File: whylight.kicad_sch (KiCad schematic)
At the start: 84 parts, among them J1 USB device, J2 External 12v, J3 LoRa, J4 I2C, J5 UART, J6 LED strip, U1 AG5412, U2 KPC357NT0ATLD, U3 ESP32-C6-WROOM-1, U4 Ra-01, U5 W5500, U6 AP63203WU, U7 USBLC6-2P6, U8 74LVC1G125, U9 L78L05_SOT89, Y1 25MHz

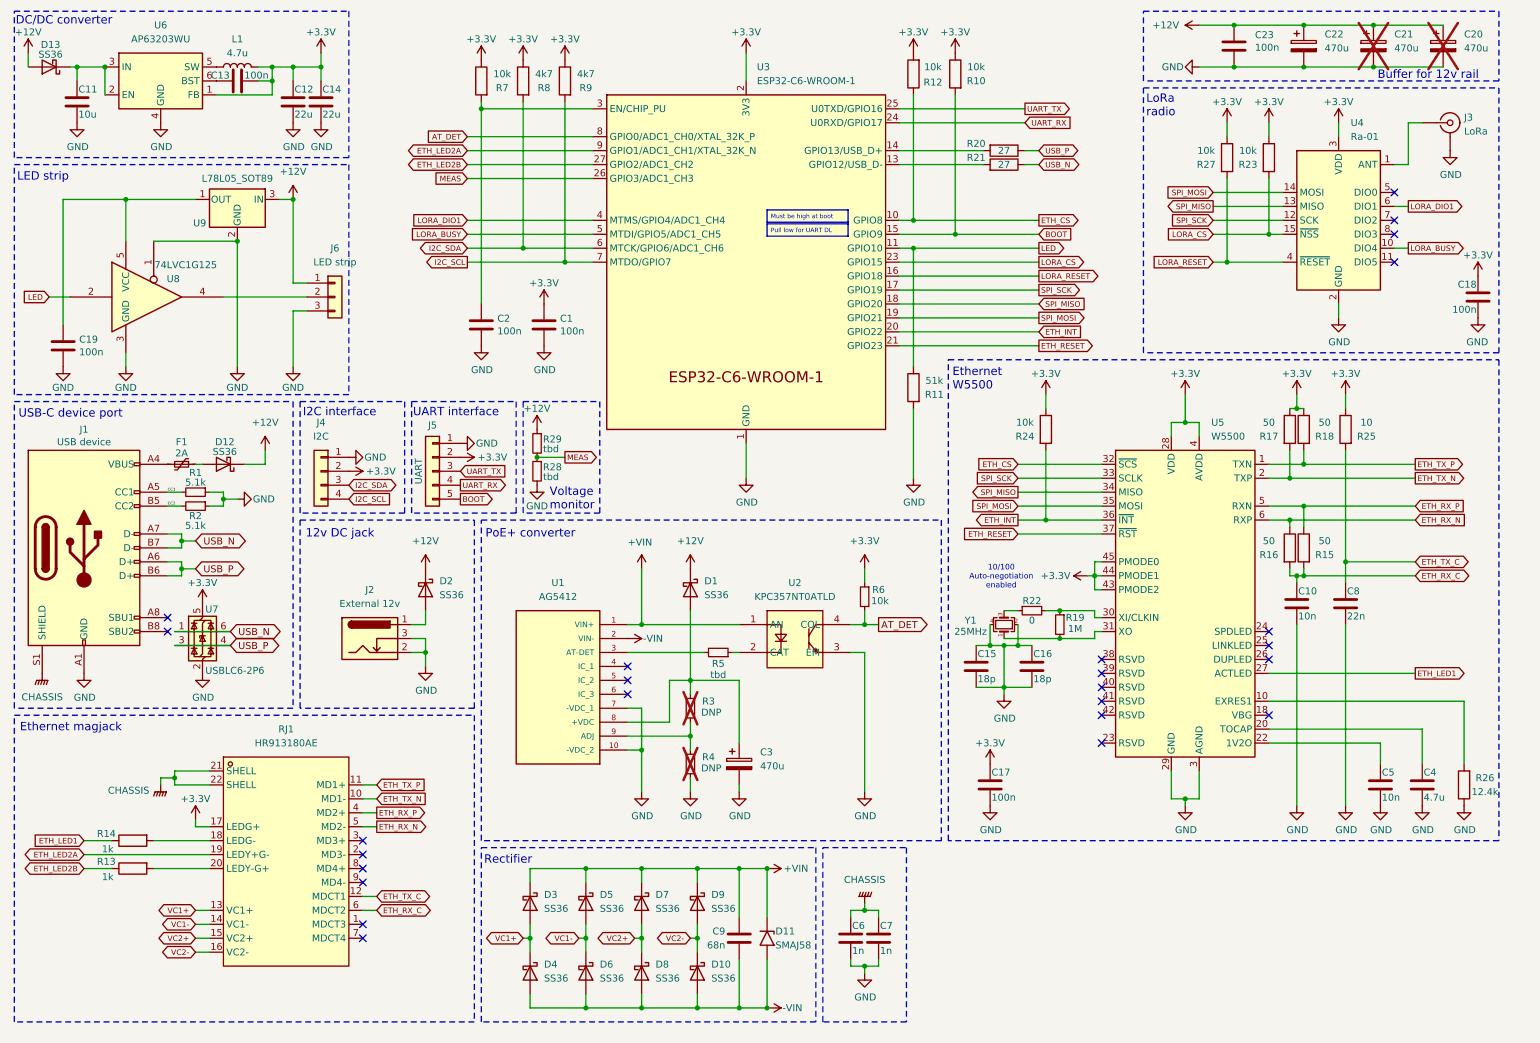
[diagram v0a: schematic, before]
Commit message: Fixes & add voltage/current monitor chip
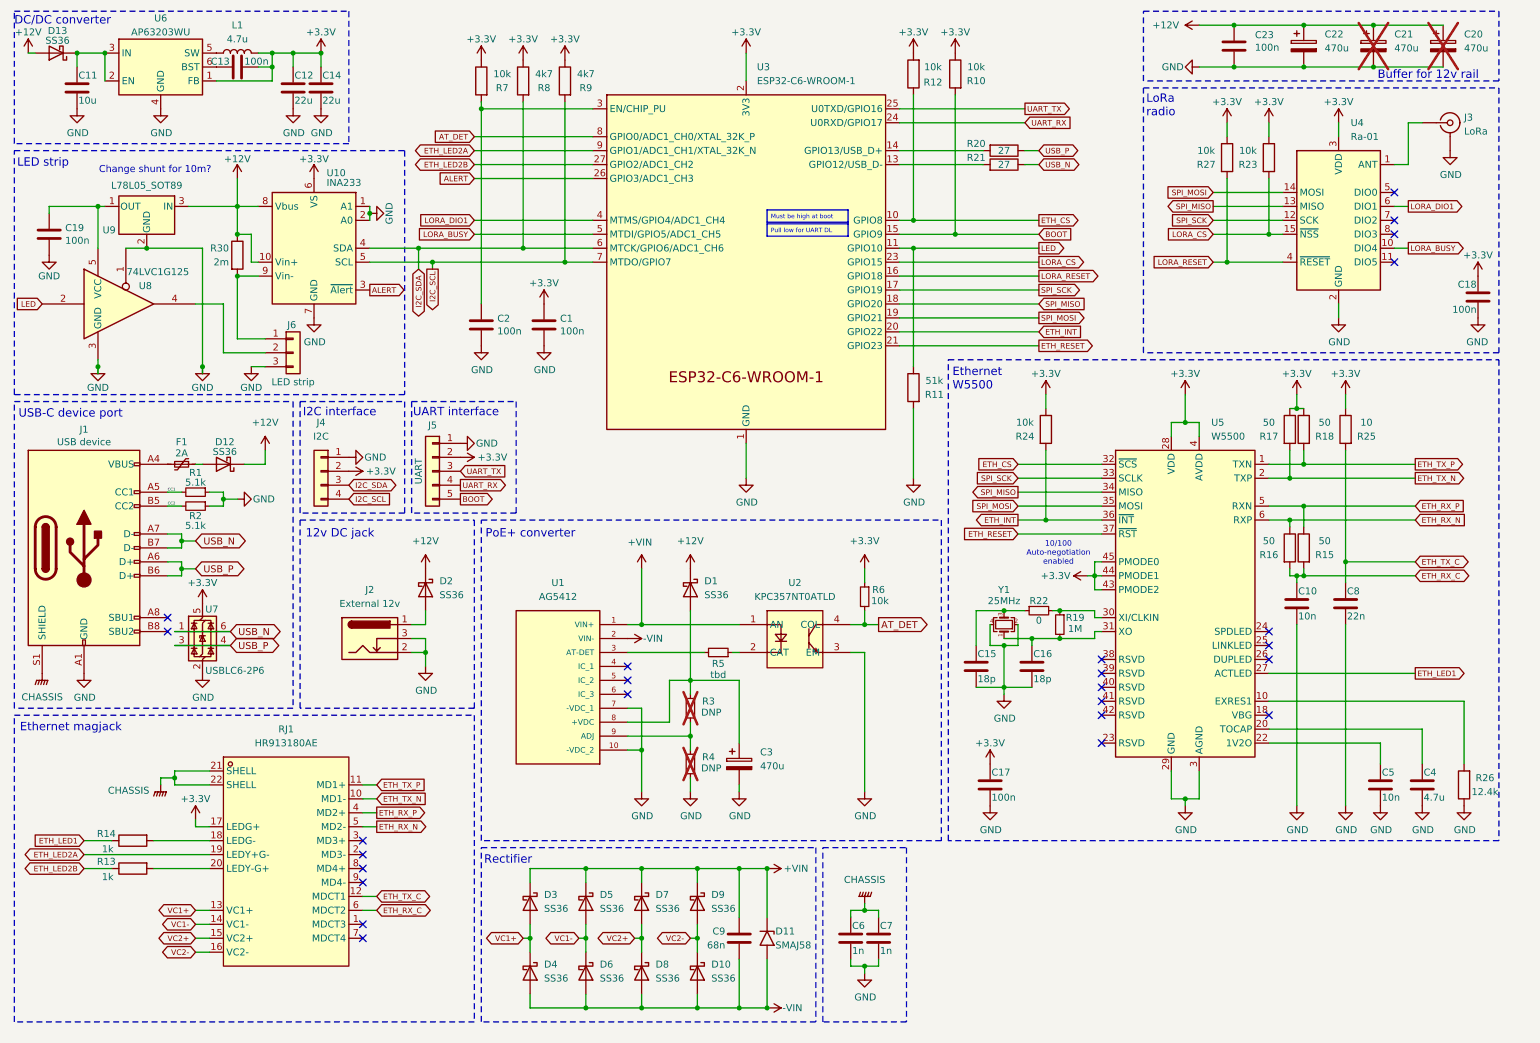
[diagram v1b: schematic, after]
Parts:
- removed R28, R29: tbd, Resistor_SMD:R_0402_1005Metric, symbol Device:R_Small
- added R30: 2m, symbol Device:R
- added U10: INA233, Package_SO:VSSOP-10_3x3mm_P0.5mm, symbol Sensor_Energy:INA233
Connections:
- net +12V: now also R30.1, U10.10 (Vin+), U10.8 (Vbus); no longer J6.1 (Pin_1)
- net +3.3V: now also U10.6 (VS)
- net GND: now also U10.1 (A1), U10.2 (A0), U10.7 (GND); no longer C15.1, C16.1
- net I2C_SCL: now also U10.5 (SCL)
- net I2C_SDA: now also U10.4 (SDA)
- net at R19.2, U5.31 (XO), Y1.1: now also C16.1
- net at R22.1, Y1.3: now also C15.1
- net MEAS renamed ALERT
- net ALERT: now also U10.3 (~{Alert})
- new net: J6.1 (Pin_1), R30.2, U10.9 (Vin-)
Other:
- note added: "Change shunt for 10m?"
- note removed: "Voltage monitor"
- moved on the sheet: C11, C12, C13, C14, C19, D13, J6, L1, R22, U6, U8, U9

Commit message: Stuff.
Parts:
- removed C10, C5: 10n, Capacitor_SMD:C_0402_1005Metric, symbol Device:C
- removed C15, C16: 18p, Capacitor_SMD:C_1206_3216Metric, symbol Device:C
- removed C17: 100n, Capacitor_SMD:C_0402_1005Metric, symbol Device:C
- removed C21, C3: 470u, symbol Device:C_Polarized
- removed C4: 4.7u, Capacitor_SMD:C_0402_1005Metric, symbol Device:C
- removed C6: 1n, Capacitor_SMD:C_1206_3216Metric, symbol Device:C
- removed C8: 22n, Capacitor_SMD:C_0402_1005Metric, symbol Device:C
- removed C9: 68n, symbol Device:C
- removed D10, D12, D13, D9: SS36, Diode_SMD:D_SMA, symbol Diode:SS36
- removed D11: SMAJ58, Diode_SMD:D_SMA, symbol Diode:SMAJ58A
- removed J2: External 12v, Connector_BarrelJack:BarrelJack_GCT_DCJ200-10-A_Horizontal, symbol Connector:Barrel_Jack_Switch
- removed J3: LoRa, SparkFun-Connector:SMA-EDGE, symbol SparkFun-RF:SMA_EdgeMount
- removed J6: LED strip, symbol Connector_Generic:Conn_01x03
- removed R13, R14: 1k, Resistor_SMD:R_0402_1005Metric, symbol symbols:R
- removed R15, R16, R17, R18: 50, Resistor_SMD:R_0402_1005Metric, symbol symbols:R
- removed R19: 1M, Resistor_SMD:R_0402_1005Metric, symbol Device:R_Small
- removed R22: 0, Resistor_SMD:R_0402_1005Metric, symbol Device:R_Small
- removed R24: 10k, Resistor_SMD:R_0402_1005Metric, symbol symbols:R
- removed R25: 10, Resistor_SMD:R_0402_1005Metric, symbol symbols:R
- removed R26: 12.4k, Resistor_SMD:R_0402_1005Metric, symbol symbols:R
- removed RJ1: HR913180AE, library:RJ45-TH_HR913180AE, symbol RJ45-TH_HR913180AE:HR913180AE
- removed U5: W5500, Package_QFP:LQFP-48_7x7mm_P0.5mm, symbol Interface_Ethernet:W5500
- removed U9: L78L05_SOT89, Package_TO_SOT_SMD:SOT-89-3, symbol Regulator_Linear:L78L05_SOT89
- removed Y1: 25MHz, Crystal:Crystal_SMD_3225-4Pin_3.2x2.5mm, symbol Device:Crystal_GND24_Small
- added C21, C24: 100n, Capacitor_SMD:C_0402_1005Metric, symbol symbols:C
- added C3: 68n, Capacitor_SMD:C_0402_1005Metric, symbol Device:C
- added C9: 470u, Capacitor_SMD:CP_Elec_8x10, symbol Device:C_Polarized
- added D10, D11: TVS, symbol SparkFun-DiscreteSemi:D_TVS
- added D9: SMAJ58, Diode_SMD:D_SMA, symbol Diode:SMAJ58A
- added F2: 10A, Fuse:Fuse_0805_2012Metric, symbol mch2021-rescue:Polyfuse_Small-Device
- added J2: External 5v, TerminalBlock_Altech:Altech_AK100_1x02_P5.00mm, symbol Connector:Screw_Terminal_01x02
- added J3: External 5v, Connector_BarrelJack:BarrelJack_GCT_DCJ200-10-A_Horizontal, symbol Connector:Barrel_Jack_Switch
- added J6: LoRa, Connector_Coaxial:SMA_Amphenol_901-143_Horizontal, symbol Connector:Conn_Coaxial
- added J7: Ledstrip, TerminalBlock_Altech:Altech_AK100_1x04_P5.00mm, symbol Connector:Screw_Terminal_01x04
- added JP1: Power source, symbol Jumper:Jumper_3_Open
- added JP2: LED logic, symbol Jumper:Jumper_3_Open
- added R28: 51k, Resistor_SMD:R_0402_1005Metric, symbol symbols:R
- added R29: 100, Resistor_SMD:R_0402_1005Metric, symbol symbols:R
- added U11: L78L05_SOT89, Package_TO_SOT_SMD:SOT-89-3, symbol Regulator_Linear:L78L05_SOT89
- added U9: 74LVC1G125, Package_TO_SOT_SMD:SOT-353_SC-70-5, symbol buffer:74LVC1G125
- C1, C19: LCSC C307331 -> C394158
- C11: value 10u -> 22u
- C13, C18, C23: LCSC (none) -> C394158
- C2: value 100n -> 1u; LCSC C307331 -> C5137485
- C20: footprint (none) -> Capacitor_SMD:CP_Elec_8x10; LCSC (none) -> C2164331; now fitted; now in the parts list
- C22: footprint (none) -> Capacitor_SMD:CP_Elec_8x10; LCSC (none) -> C2164331
- C7: LCSC (none) -> C2173292
- J4: footprint (none) -> Connector_JST:JST_SH_SM04B-SRSS-TB_1x04-1MP_P1.00mm_Horizontal; symbol Connector_Generic:Conn_01x04 -> Connector_Generic_MountingPin:Conn_01x04_MountingPin
- J5: footprint (none) -> Connector_PinHeader_2.54mm:PinHeader_1x06_P2.54mm_Vertical; symbol Connector_Generic:Conn_01x05 -> Connector_Generic:Conn_01x06
- R23: value 10k -> 1k
- R27: value 10k -> 100
- R30: value 2m -> 10m; footprint (none) -> Resistor_SMD:R_1206_3216Metric
- R5: value tbd -> 1k
- R6, R7: LCSC (none) -> C60490
- U1: value AG5412 -> AG5405; Availability In Stock -> (none); Check_prices https://www.snapeda.com/parts/Ag5300/Silvertel/view-part/?r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 -> (none); DESCRIPTION Power-over-Ethernet Plus Module -> (none); Description_1 Isolated PoE Module DC DC Converter Output 12V 2.5A 36V - 5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 -> (none); HEIGHT 14mm -> (none); MANUFACTURER_NAME Silvertel -> (none); MANUFACTURER_PART_NUMBER AG5300 -> (none); MF Silvertel -> (none); MOUSER_PART_NUMBER 480-AG5300 -> (none); MOUSER_PRICE-STOCK https://www.mouser.co.uk/ProductDetail/Silvertel/Ag5300?qs=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 -> (none); MP Ag5300 -> (none); Package None -> (none); Price None -> (none); Purchase-URL https://www.snapeda.com/api/url_track_click_mouser/?unipart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 -> (none); SnapEDA_Link https://www.snapeda.com/parts/Ag5300/Silvertel/view-part/?r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 -> (none)
- U2: LCSC (none) -> C136410; LCSC Part C136410 -> (none)
- U8: symbol 74xGxx:74LVC1G125 -> buffer:74LVC1G125
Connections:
- net -VIN is gone; now on an unnamed net: D4.2 (A), D6.2 (A), D8.2 (A), U1.2 (VIN-)
- net +3.3V: no longer R23.1, R27.1
- net +VIN: now also R30.1, U10.10 (Vin+), U10.8 (Vbus), D10.1 (A1), F2.1, JP1.3 (B), U11.3 (IN); no longer D3.1 (K), D5.1 (K), D7.1 (K), U1.1 (VIN+), U2.1 (AN)
- net AT_DET: now also U3.11 (GPIO10); no longer U3.8 (GPIO0/ADC1_CH0/XTAL_32K_P)
- net ETH_INT: now also U3.4 (MTMS/GPIO4/ADC1_CH4); no longer U3.20 (GPIO22)
- net ETH_LED2A: now also R11.1, U3.17 (GPIO19); no longer U3.9 (GPIO1/ADC1_CH1/XTAL_32K_N)
- net GND: now also C19.1, J4.MP (MountPin), C21.2, C24.1, C9.2, D10.2 (A2), D11.2 (A2), J2.1 (Pin_1), J3.2, J3.3, J6.2 (Ext), J7.4 (Pin_4), R28.2, U11.2 (GND), U9.1, U9.3 (GND); no longer C19.2
- net LORA_BUSY: now also U3.19 (GPIO21); no longer U3.5 (MTDI/GPIO5/ADC1_CH5)
- net LORA_CS: no longer R23.2
- net LORA_DIO1: now also U3.20 (GPIO22); no longer U3.4 (MTMS/GPIO4/ADC1_CH4)
- net LORA_RESET: now also R28.1; no longer R27.2
- net SPI_MISO: now also U3.8 (GPIO0/ADC1_CH0/XTAL_32K_P); no longer U3.18 (GPIO20)
- net SPI_MOSI: now also U3.5 (MTDI/GPIO5/ADC1_CH5); no longer U3.19 (GPIO21)
- net SPI_SCK: now also U3.9 (GPIO1/ADC1_CH1/XTAL_32K_N); no longer U3.17 (GPIO19)
- net UART_RX: now also R23.1; no longer U3.24 (U0RXD/GPIO17)
- net VC1+: now also D1.2 (A), D2.1 (K); no longer D3.2 (A), D4.1 (K)
- net VC1-: now also D3.2 (A), D4.1 (K); no longer D5.2 (A), D6.1 (K)
- net VC2+: now also D5.2 (A), D6.1 (K); no longer D7.2 (A), D8.1 (K)
- net VC2-: now also D7.2 (A), D8.1 (K)
- net VLED: now reaches R30.2, U10.9 (Vin-)
- net VLED: now also C20.1, C22.1, C23.1, J7.1 (Pin_1)
- net at U8.4: now also R29.1
- net at C11.1, U6.2 (EN), U6.3 (IN): now also JP1.2 (C)
- net at R3.2, U1.8 (+VDC): now also C9.1, F2.2, J2.2 (Pin_2), J3.1; no longer D1.2 (A)
- net +5V: now reaches U8.5 (VCC)
- net +5V: now also C19.2, C24.2, JP2.2 (C), U9.5 (VCC); no longer C19.1
- net at D2.2 (A): now also C3.2, D9.2 (A2)
- net at U4.1 (ANT): now also J6.1 (In)
- net +5v-USB: now reaches F1.1
- net +5v-USB: now also D11.1 (A1), JP1.1 (A), JP2.3 (B)
- net EN: now reaches C2.1, R7.2, U3.3 (EN/CHIP_PU)
- net EN: now also J5.6 (Pin_6)
- removed net +12V: C20.1, C22.1, C23.1, D1.1 (K), D2.1 (K), R30.1, U10.10 (Vin+), U10.8 (Vbus)
- net CHASSIS: no longer names the net of C7.1, J1.S1 (SHIELD)
- removed net LED: R11.1, U3.11 (GPIO10), U8.2
- new net: C21.1, JP2.1 (A), U11.1 (OUT)
- new net: J7.3 (Pin_3), R27.1
- new net: R27.2, U9.4
- new net: J7.2 (Pin_2), R29.2
- new net: C3.1, D1.1 (K), D3.1 (K), D5.1 (K), D7.1 (K), D9.1 (A1), U1.1 (VIN+), U2.1 (AN)
- new net LCLK: R23.2, U3.24 (U0RXD/GPIO17), U9.2
- new net LDAT: U3.18 (GPIO20), U8.2
- no-connect marks 25 -> 9
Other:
- added sheet Ethernet (ethernet.kicad_sch)
- note added: "Choose between USB and ext / PoE power"
- note added: "DC/DC converter for logic"
- note added: "Do NOT backfeed power into the PoE module. Install only one of the connectors or the PoE module but not multiple!"
- note added: "Ethernet"
- note added: "I2C & UART"
- note added: "LDO for LED data logic voltage"
- note added: "Microcontroller"
- note added: "PoE+ & external power"
- note added: "Power measurement"
- note removed: "10/100 Auto-negotiation enabled"
- note removed: "12v DC jack"
- note removed: "Buffer for 12v rail"
- note removed: "Change shunt for 10m?"
- note removed: "DC/DC converter"
- note removed: "Ethernet W5500"
- note removed: "Ethernet magjack"
- note removed: "I2C interface"
- note removed: "LED strip"
- note removed: "PoE+ converter"
- note removed: "Rectifier"
- note removed: "UART interface"
- moved on the sheet: C1, C12, C13, C14, C18, C19, C2, C22, C23, F1, J1, L1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

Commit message: Stuff.
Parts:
- removed F2: 10A, Fuse:Fuse_0805_2012Metric, symbol mch2021-rescue:Polyfuse_Small-Device
- removed J6: LoRa, Connector_Coaxial:SMA_Amphenol_901-143_Horizontal, symbol Connector:Conn_Coaxial
- C11, C12, C14: footprint Capacitor_SMD:C_0402_1005Metric -> Capacitor_SMD:C_0805_2012Metric; LCSC (none) -> C45783
- D1, D2, D3, D4, D5, D6, D7, D8: LCSC (none) -> C727061
- D10, D11: value TVS -> 5.5v; footprint (none) -> Diode_SMD:D_SOD-323; LCSC (none) -> C19224
- D9: LCSC (none) -> C132935
- J2: footprint TerminalBlock_Altech:Altech_AK100_1x02_P5.00mm -> Connector_Phoenix_MC_HighVoltage:PhoenixContact_MC_1,5_2-G-5.08_1x02_P5.08mm_Horizontal; LCSC (none) -> -; now not fitted; now left out of the parts list
- J3, J5, U1: LCSC (none) -> -; now not fitted; now left out of the parts list
- J4: LCSC (none) -> C160404
- J7: footprint TerminalBlock_Altech:Altech_AK100_1x04_P5.00mm -> Connector_Phoenix_MC_HighVoltage:PhoenixContact_MC_1,5_4-GF-5.08_1x04_P5.08mm_Horizontal_ThreadedFlange_MountHole; LCSC (none) -> -; now not fitted; now left out of the parts list
- JP1, JP2: footprint (none) -> Jumper:SolderJumper-3_P1.3mm_Open_RoundedPad1.0x1.5mm_NumberLabels; LCSC (none) -> -
- U10: LCSC (none) -> C2653838
- U11: LCSC (none) -> C408272
- U4: value Ra-01 -> Ra-01SH; LCSC (none) -> -; now not fitted; now left out of the parts list
- U6: LCSC (none) -> C780769
- U7: LCSC (none) -> C2827693
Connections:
- net +VIN: now also C9.1, J2.2 (Pin_2), J3.1, R3.2, U1.8 (+VDC)
- no-connect marks 9 -> 10
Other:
- note added: "U.FL connector on-board"

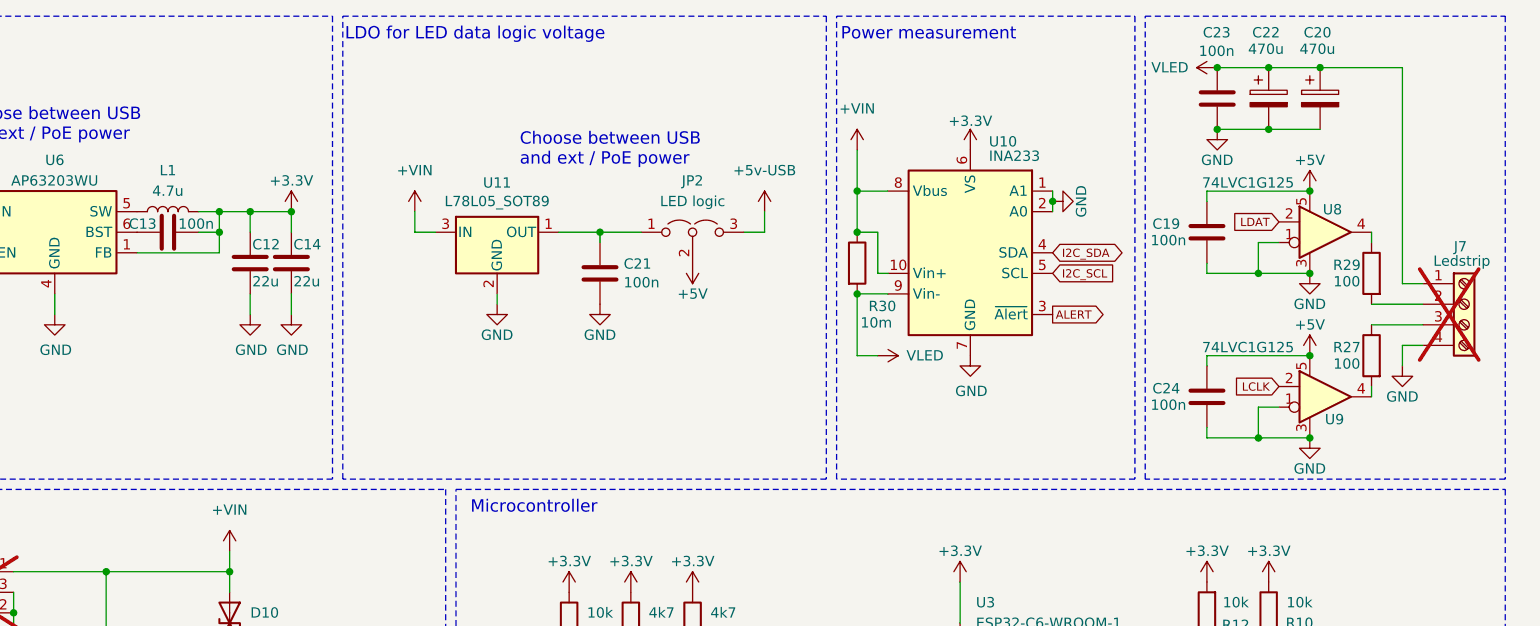
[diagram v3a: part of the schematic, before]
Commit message: added 3D models, added LCSC numbers, added caps in RX line ethernet as per the datasheet, change crystal and capacitors to correctly match w5500 as per the datasheet, added bead to filter analoge power supply for w5500 as per the datasheet, added filter for the ina2XX for beter monitoring
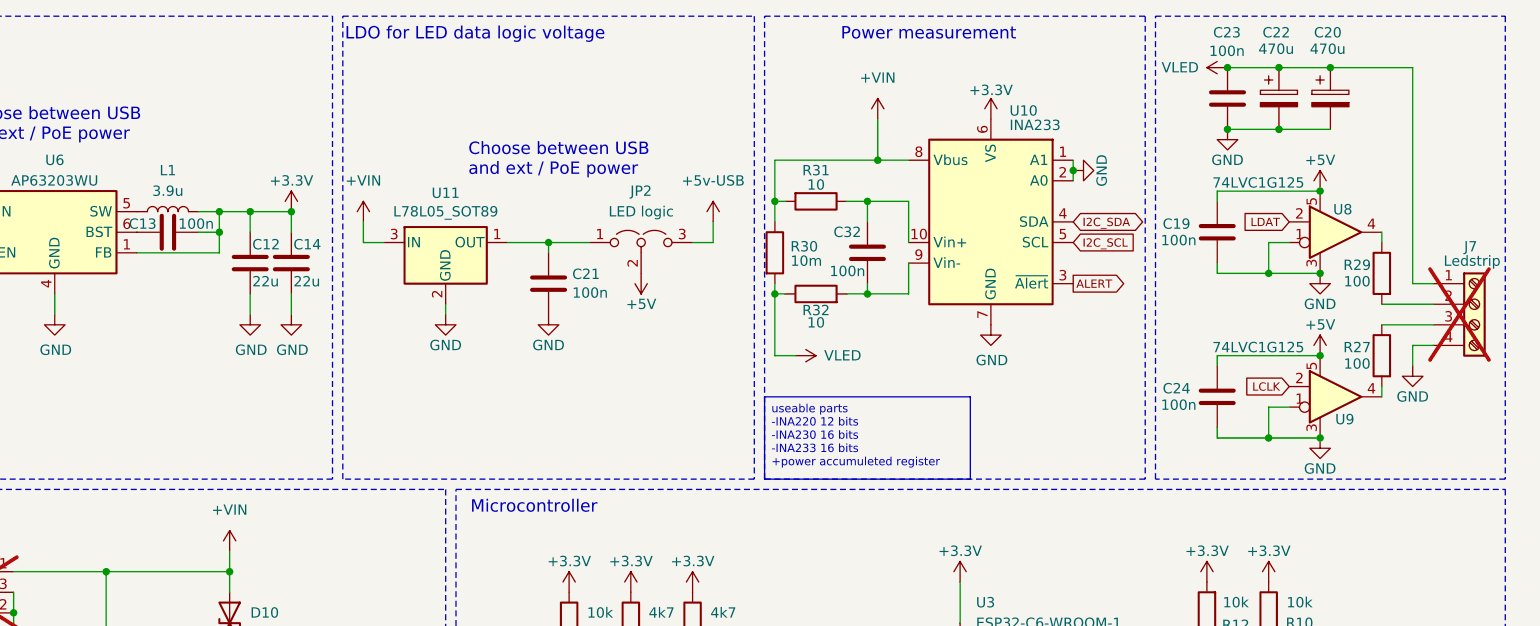
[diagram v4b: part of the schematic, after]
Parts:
- added C32: 100n, Capacitor_SMD:C_0402_1005Metric, symbol symbols:C
- added R31, R32: 10, Resistor_SMD:R_0402_1005Metric, symbol symbols:R
- J2: LCSC - -> C5188463
- J3: LCSC - -> C381116; MOUSER (none) -> 640-DCJ200-10-A-K1-K
- L1: value 4.7u -> 3.9u; footprint (none) -> Inductor_SMD:L_Coilcraft_XAL5050-XXX; LCSC (none) -> C7427114
- R23, R5: LCSC (none) -> C2935237
- R27, R29: LCSC (none) -> C25076
- R3, R4: LCSC (none) -> -
- R30: LCSC (none) -> C105362
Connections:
- net +VIN: now also R31.2; no longer U10.10 (Vin+)
- net VLED: now also R32.1; no longer U10.9 (Vin-)
- new net: C32.2, R31.1, U10.10 (Vin+)
- new net: C32.1, R32.2, U10.9 (Vin-)
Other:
- moved on the sheet: C19, C20, C21, C22, C23, C24, J7, JP2, R27, R29, R30, U10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

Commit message: Change pinout of C6 to more closely resemble the WHY2025 badge
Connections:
- net ALERT: now also U3.23 (GPIO15); no longer U3.26 (GPIO3/ADC1_CH3)
- net ETH_INT: now also U3.19 (GPIO21); no longer U3.4 (MTMS/GPIO4/ADC1_CH4)
- net ETH_LED2B: now also U3.20 (GPIO22); no longer U3.27 (GPIO2/ADC1_CH2)
- net LORA_BUSY: now also U3.5 (MTDI/GPIO5/ADC1_CH5); no longer U3.19 (GPIO21)
- net LORA_CS: now also U3.9 (GPIO1/ADC1_CH1/XTAL_32K_N); no longer U3.23 (GPIO15)
- net LORA_DIO1: now also U3.4 (MTMS/GPIO4/ADC1_CH4); no longer U3.20 (GPIO22)
- net SPI_MISO: now also U3.26 (GPIO3/ADC1_CH3); no longer U3.8 (GPIO0/ADC1_CH0/XTAL_32K_P)
- net SPI_MOSI: now also U3.27 (GPIO2/ADC1_CH2); no longer U3.5 (MTDI/GPIO5/ADC1_CH5)
- net SPI_SCK: now also U3.8 (GPIO0/ADC1_CH0/XTAL_32K_P); no longer U3.9 (GPIO1/ADC1_CH1/XTAL_32K_N)
